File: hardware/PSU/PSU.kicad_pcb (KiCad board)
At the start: 2 copper layers, 28 x 110 mm, 27 parts, among them CN1 JST PH 2 pin male, CN2 JST PH 2 pin male, J1 IDC 2x5 male, J2 IDC 2x5 male, U1 K7812, U2 K7812

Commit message: Add test points
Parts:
- added TP1: GND, TestPoint:TestPoint_Keystone_5000-5004_Miniature, F.Cu at (74.0, 60.0)
- added TP2: GND, TestPoint:TestPoint_Keystone_5000-5004_Miniature, F.Cu at (72.0, 95.0)
- added TP3: +12v, TestPoint:TestPoint_Keystone_5000-5004_Miniature, F.Cu at (72.0, 100.0)
- added TP4: -12v, TestPoint:TestPoint_Keystone_5000-5004_Miniature, F.Cu at (72.0, 105.0)
- added TP5: +15v, TestPoint:TestPoint_Keystone_5000-5004_Miniature, F.Cu at (74.0, 64.0)
- U1, U2: value K7812 -> K7812-1000R3
- moved H3 122.2 mm to (54.0, 156.0)
- moved H4 102.5 mm to (74.0, 156.0)
- moved H1 88.6 mm to (54.0, 54.0)
- moved H2 69.3 mm to (74.0, 54.0)
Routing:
- net -12V: track 82.2 -> 126.8 mm, vias 1 -> 0
- net +15V: track 65.2 -> 74.9 mm
- net +12V: track 88.1 -> 94.7 mm

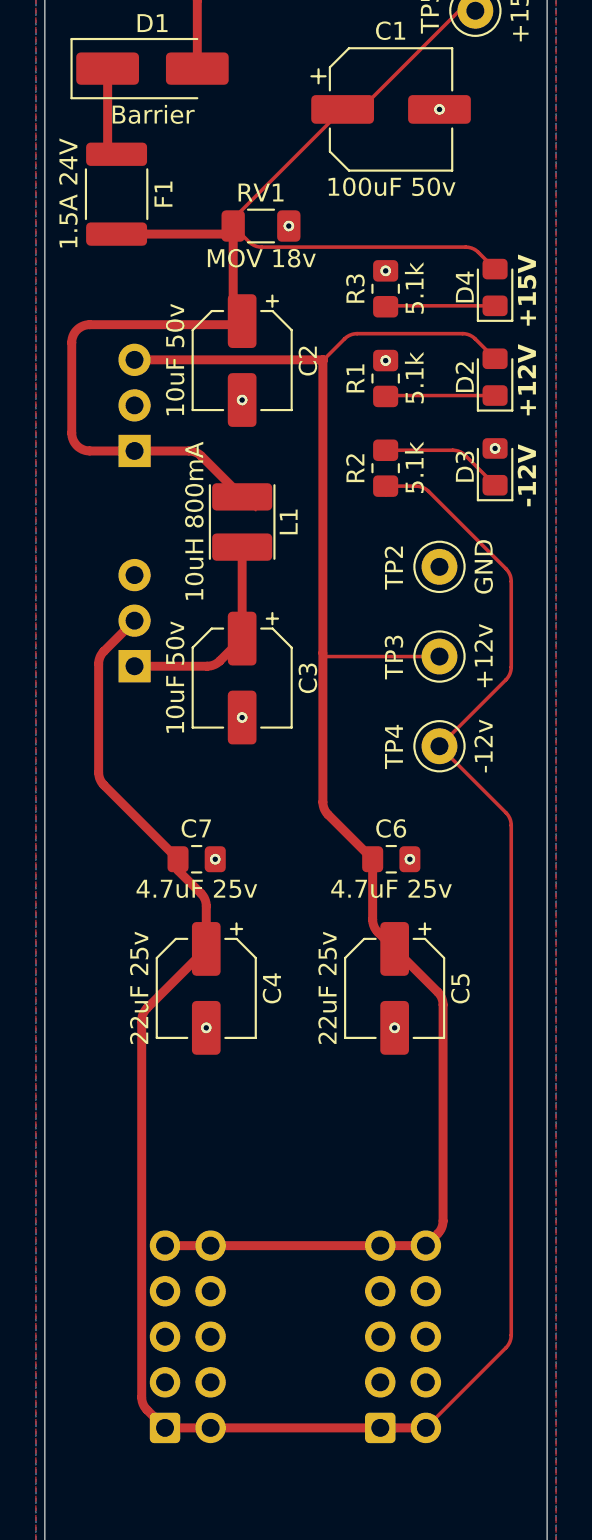
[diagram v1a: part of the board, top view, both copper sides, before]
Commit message: Use 3mm LEDs instead
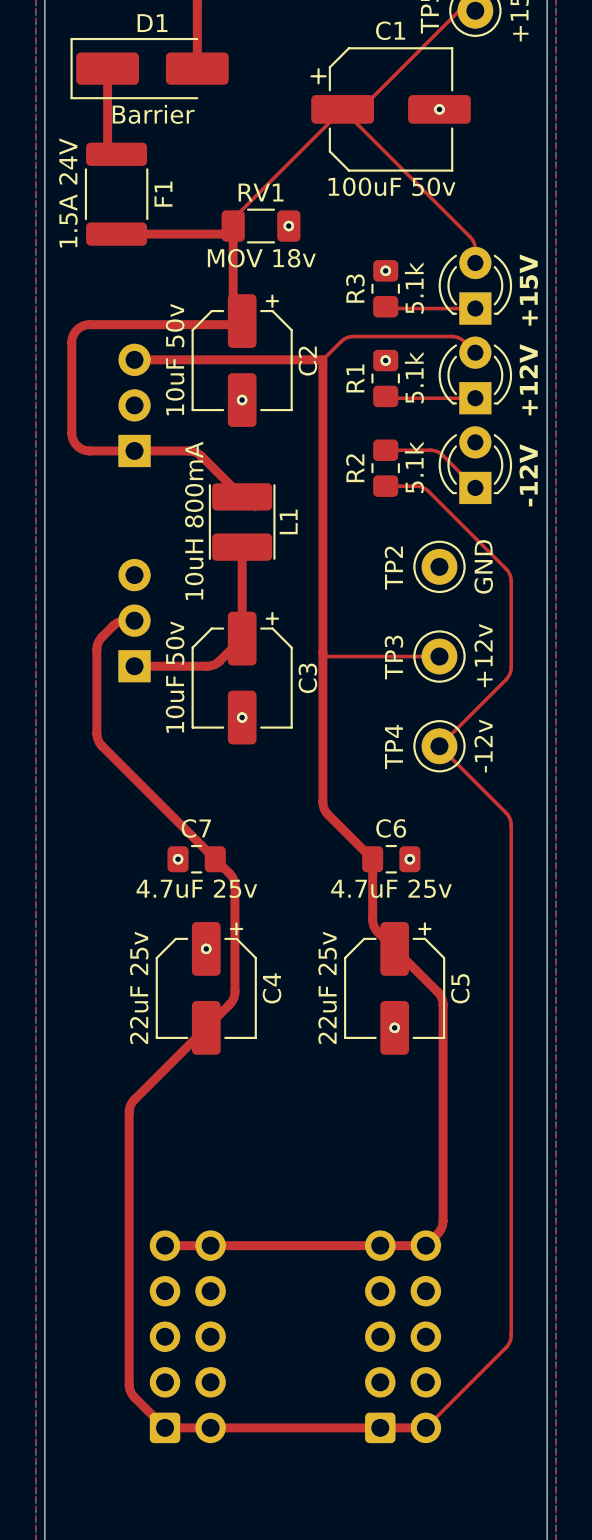
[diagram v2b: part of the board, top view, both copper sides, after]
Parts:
- D2, D3, D4: footprint LED_SMD:LED_0805_2012Metric_Pad1.15x1.40mm_HandSolder -> LED_THT:LED_D3.0mm
- moved D2 1.61 mm to (74.0, 85.6)
- moved D3 1.61 mm to (74.0, 90.6)
- moved D4 1.61 mm to (74.0, 80.6)
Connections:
- C4 pad 1: -12V -> GND
- C4 pad 2: GND -> -12V
- C7 pad 1: -12V -> GND
- C7 pad 2: GND -> -12V
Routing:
- net +15V: track 74.9 -> 71.0 mm
- net -12V: track 126.8 -> 129.2 mm
- net +12V: track 94.7 -> 93.3 mm
- net Net-(D3-K): track 6.86 -> 5.82 mm
- net Net-(D2-K): track 6.12 -> 5.11 mm
- net Net-(D4-K): track 6.19 -> 5.68 mm
- net GND: vias 11 -> 10
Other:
- board text removed: "-12v"

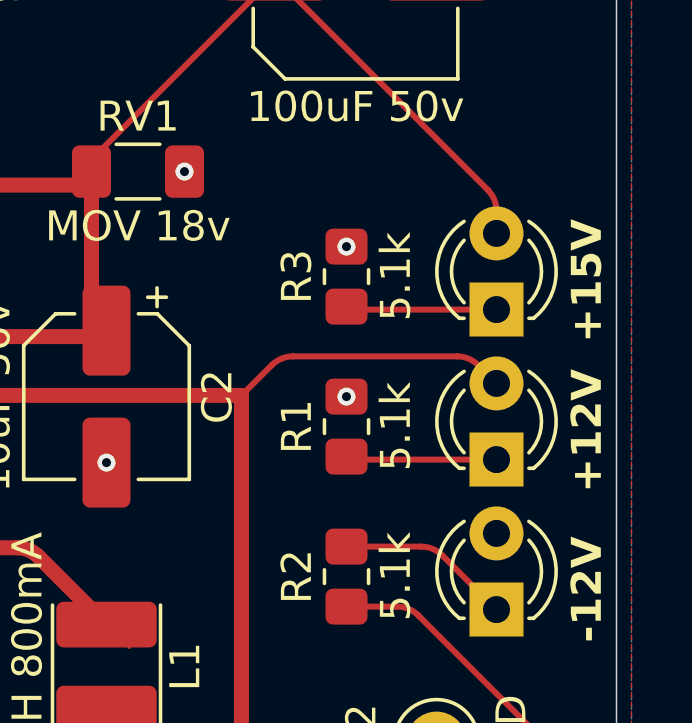
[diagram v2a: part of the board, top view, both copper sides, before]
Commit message: Add + markers
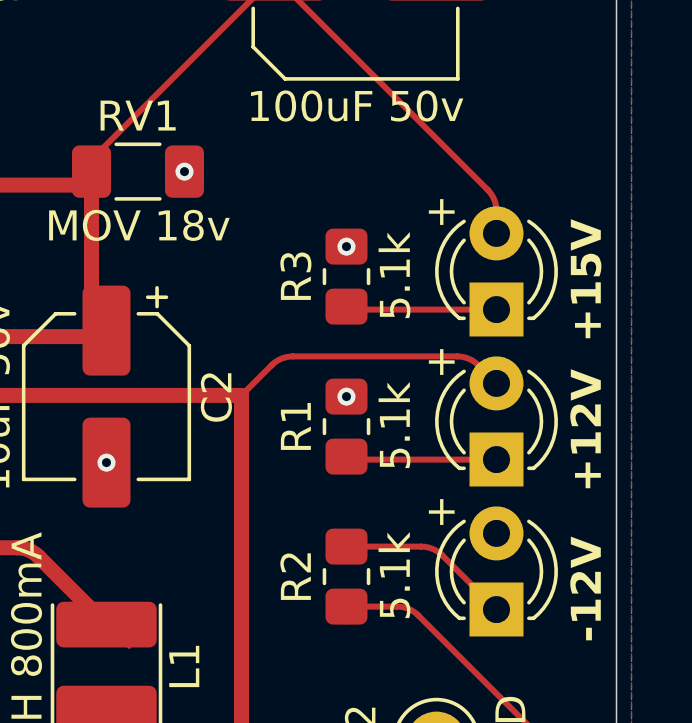
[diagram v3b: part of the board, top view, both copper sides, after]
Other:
- board text added: "+"
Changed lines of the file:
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@@
+		)
+	)
+	(gr_text "+"
+		(at 71.6 87.9 0)
+		(layer "F.SilkS")
+		(effects
+			(font
+				(size 1 1)
+				(thickness 0.125)
+			)
+			(justify left bottom)
+		)
+	)
+	(gr_text "+"
+		(at 71.6 77.9 0)
+		(layer "F.SilkS")
+		(effects
+			(font
+				(size 1 1)
+				(thickness 0.125)
+			)
+			(justify left bottom)
 		)
 	)
@@
 				(thickness 0.2)
 				(bold yes)
+			)
+			(justify left bottom)
+		)
+	)
+	(gr_text "+"
+		(at 71.6 82.9 0)
+		(layer "F.SilkS")
+		(effects
+			(font
+				(size 1 1)
+				(thickness 0.125)
 			)
 			(justify left bottom)
@@
 			)
 			(justify left bottom mirror)
+		)
+	)
+	(gr_text "+"
+		(at 61.6 62.5 0)
+		(layer "B.SilkS")
+		(effects
+			(font
+				(size 1 1)
+				(thickness 0.125)
+			)
+			(justify left bottom mirror)
+		)
+	)
+	(gr_text "+"
+		(at 71.6 62.5 0)
+		(layer "B.SilkS")
+		(effects
+			(font
+				(size 1 1)
+				(thickness 0.125)
+			)
+			(justify left bottom mirror)

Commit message: Add more labels to the power input connections
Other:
- board text added: "-"
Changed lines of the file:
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@@
+		)
+	)
+	(gr_text "-"
+		(at 71.6 60.4 0)
+		(layer "B.SilkS")
+		(effects
+			(font
+				(size 1 1)
+				(thickness 0.125)
+			)
+			(justify left bottom mirror)
+		)
+	)
+	(gr_text "-"
+		(at 61.6 60.5 0)
+		(layer "B.SilkS")
+		(effects
+			(font
+				(size 1 1)
+				(thickness 0.125)
+			)
+			(justify left bottom mirror)
 		)
 	)
